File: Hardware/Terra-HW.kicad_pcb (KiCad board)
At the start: 4 copper layers, 77 x 68 mm, 97 parts, among them J1 GT-USB-7010ASV, J2 S2B-PH-SM4-TB, J3 0532610271, J5 B8B-PH-SM4-TB, J6 0532610671, Q1 DMP3099L, Q2 2N7002, Q3 2N7002, SW2 KMR231NG, SW3 KMR231NG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

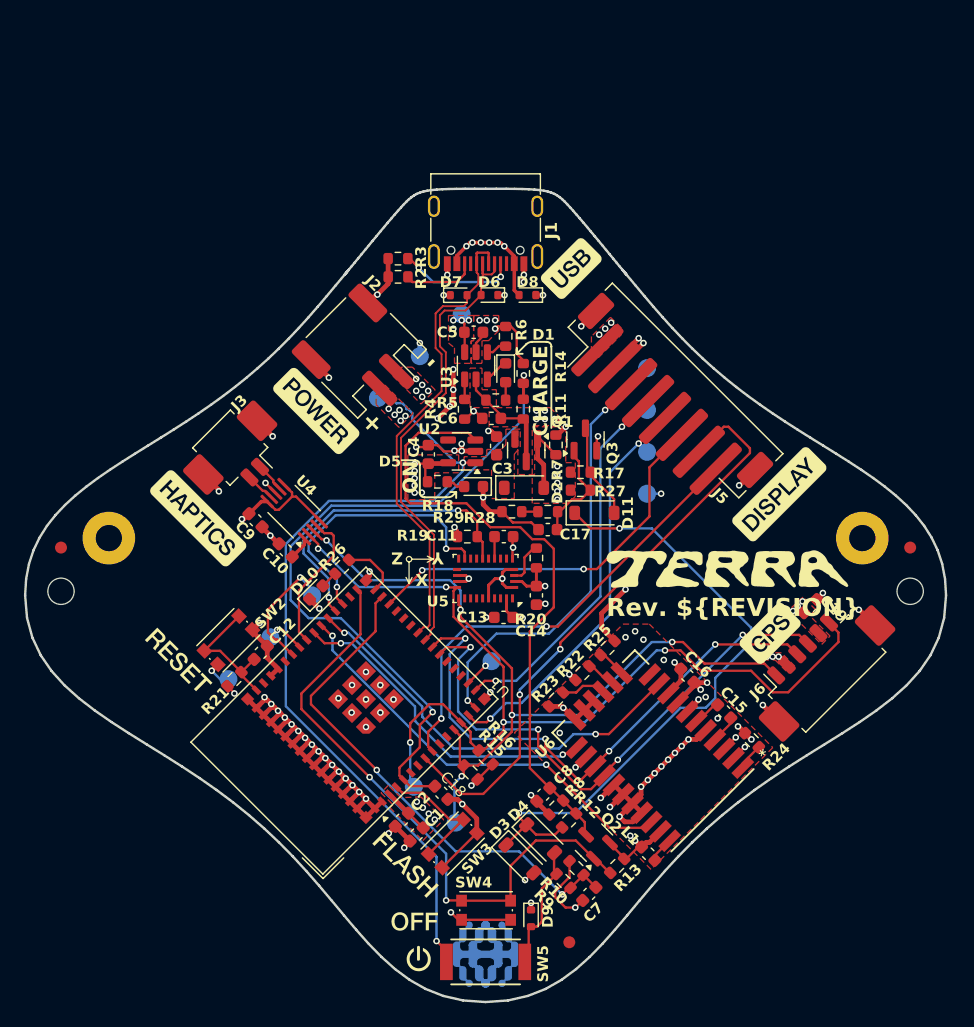
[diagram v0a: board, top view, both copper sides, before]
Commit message: update board outline and flip 180
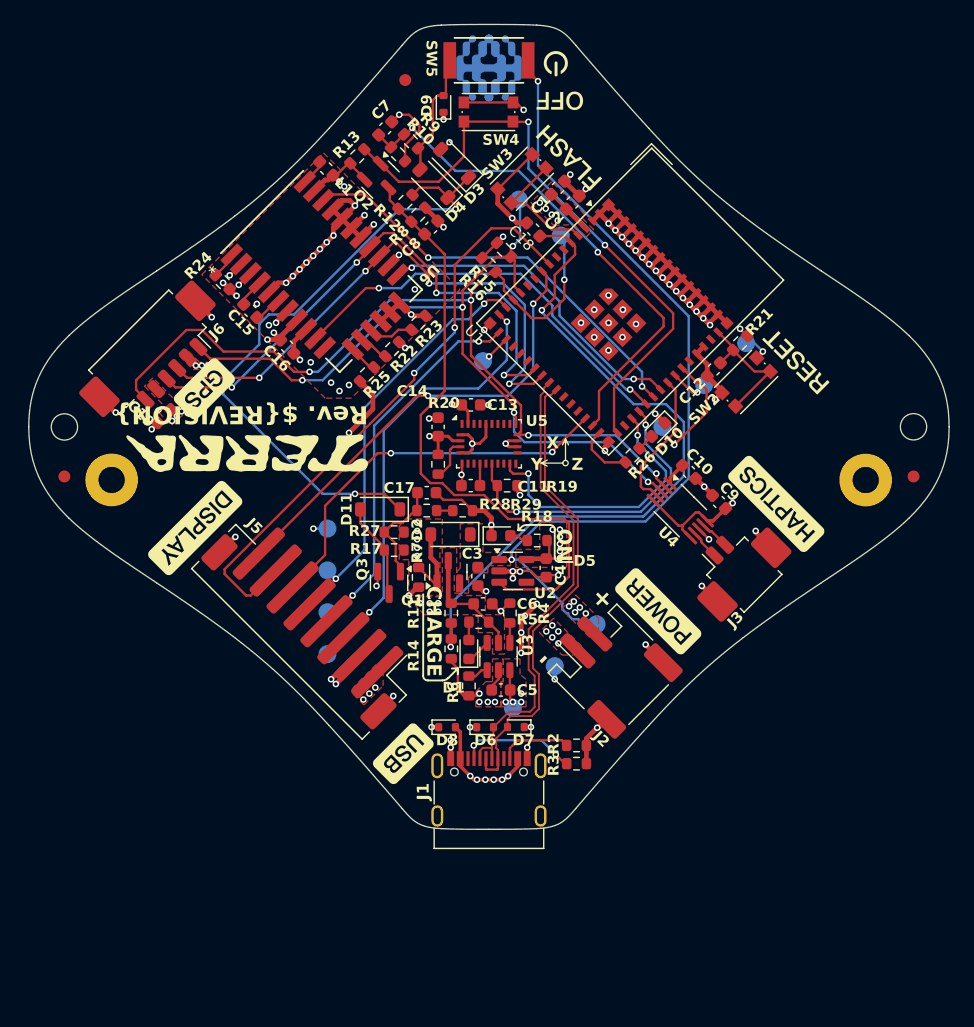
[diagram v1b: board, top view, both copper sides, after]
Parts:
- moved SW5 75.4 mm to (150.0, 61.4), turned to 180 degrees
- moved FID2 73.4 mm to (143.0, 63.1), turned to 180 degrees
- moved H2 72.6 mm to (185.5, 92.1), turned to 180 degrees
- moved H1 72.0 mm to (114.6, 92.1), turned to 180 degrees
- moved FID3 71.5 mm to (185.5, 96.2), turned to 180 degrees
- moved FID1 71.0 mm to (114.5, 96.2), turned to 180 degrees
- moved D9 68.5 mm to (146.2, 65.1), turned to 90 degrees
- moved SW4 66.7 mm to (150.0, 65.7), turned to 0 degrees
- moved C7 66.2 mm to (141.4, 67.1), turned to 45 degrees
- moved H3 63.5 mm to (181.5, 96.5), turned to 180 degrees
- moved L1 63.3 mm to (136.4, 70.5), turned to -45 degrees
- moved R13 63.2 mm to (139.0, 69.4), turned to 45 degrees
- moved R9 63.1 mm to (143.5, 68.2), turned to -45 degrees
- moved H4 62.9 mm to (118.5, 96.5), turned to 180 degrees
- moved J6 62.0 mm to (121.8, 85.9), turned to -135 degrees
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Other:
- board size 77 x 68 mm -> 76.9 x 67.3 mm

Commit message: pcb: initial layout of TESSO gps
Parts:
- removed J6: 0532610671, Connector_Molex:Molex_PicoBlade_53261-0671_1x06-1MP_P1.25mm_Horizontal
- removed R23: 10k, Resistor_SMD:R_0603_1608Metric
- removed R24: 0R, Resistor_SMD:R_0603_1608Metric
- added J4: Conn_Coaxial, Connector_Coaxial:U.FL_Molex_MCRF_73412-0110_Vertical, F.Cu at (123.7, 83.6)
- added U7: BGA725L6, Symbols:BGA-6_2x3_0.8x1.2mm, F.Cu at (129.4, 86.0)
- added U8: B4327, Symbols:SOIC-5 B4327, F.Cu at (128.3, 84.7)
- C15, C16: value 22p -> 120p; footprint Capacitor_SMD:C_0603_1608Metric -> Capacitor_SMD:C_0402_1005Metric
- C19: value 1u -> 0.1u
- L1: value 1.8n -> 5.6n; footprint Inductor_SMD:L_0603_1608Metric -> Inductor_SMD:L_0402_1005Metric
- U6: value M20048-1 -> TESEO-LIV3F; footprint M20048-1:QFN28_M20048-1_ANT -> TESO-LIV3F:LCC-18_9P7X10P1_STM
- moved L1 19.2 mm to (127.5, 87.5)
- moved C19 11.4 mm to (130.8, 83.0), turned to -45 degrees
- moved R22 9.98 mm to (132.0, 85.6), turned to -135 degrees
- moved C16 7.14 mm to (126.1, 86.0), turned to 135 degrees
- moved C15 2.94 mm to (127.2, 82.8)
- moved U6 1.75 mm to (134.6, 78.0), turned to -135 degrees
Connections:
- C15 pad 1: Net-(U6-ANT_OUT) -> Net-(U6-RF_IN)
- C15 pad 2: Net-(U6-RF_IN) -> Net-(U8-RF_{OUT})
- C16 pad 1: +3.3V -> Net-(C16-Pad1)
- C16 pad 2: GND -> Net-(J4-In)
- C19 pad 1: +3.3V -> +3.3V_RF
- J2 pad 1: GND -> VBAT
- J2 pad 2: VBAT -> GND
- L1 pad 1: Net-(U6-AT2) -> Net-(C16-Pad1)
- L1 pad 2: GND -> Net-(U7-A_{IN})
- R22 pad 1: /Peripehrals/GPS_BAUD1 -> GND
- R22 pad 2: GND -> /Peripehrals/ANT_EN
- R25 pad 2: /Peripehrals/GPS_VBACKUP -> /Peripehrals/GPS_VBAT
- U6 pad 1: Net-(U6-AT1) -> GND
- U6 pad 10: /Microcontroller/GPS_~{RST} -> GND
- U6 pad 11: unconnected-(U6-TM-Pad11) -> Net-(U6-RF_IN)
- U6 pad 12: /Peripehrals/GPS_VBACKUP -> GND
- U6 pad 13: /Peripehrals/GPS_BAUD1 -> /Peripehrals/ANT_EN
- U6 pad 14: /Peripehrals/GPS_BAUD2 -> +3.3V_RF
- U6 pad 15: GND -> unconnected-(U6-RESERVED-Pad15)
- U6 pad 16: GND -> /Microcontroller/I2C_SDA
- U6 pad 17: GND -> /Microcontroller/I2C_SCL
- U6 pad 18: /Microcontroller/GPS_FIX -> unconnected-(U6-RESERVED-Pad18)
- U6 pad 2: GND -> /Microcontroller/U1RXD
- U6 pad 3: GND -> /Microcontroller/U1TXD
- U6 pad 4: Net-(U6-ANT_OUT) -> /Microcontroller/GPS_FIX
- U6 pad 5: GND -> /Microcontroller/GPS_STBY
- U6 pad 6: Net-(U6-RF_IN) -> /Peripehrals/GPS_VBAT
- U6 pad 7: GND -> +3.3V
- U6 pad 9: GND -> /Microcontroller/GPS_~{RST}
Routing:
- net GND: track 192.8 -> 148.8 mm, vias 115 -> 105
- net /Microcontroller/U1TXD: track 46.7 -> 25.2 mm, vias 4 -> 2
- net /Microcontroller/U1RXD: track 46.5 -> 26.1 mm, vias 4 -> 2
- net /Microcontroller/I2C_SCL: track 79.7 -> 60.1 mm, vias 5 -> 4
- net /Peripehrals/GPS_VBAT: track 0.00 -> 10.4 mm
- net /Microcontroller/I2C_SDA: track 68.3 -> 58.5 mm, vias 5 -> 4
- net /Peripehrals/ANT_EN: track 0.00 -> 8.54 mm, vias 0 -> 3
- net Net-(D11-K): track 53.6 -> 46.0 mm
- net +3.3V_RF: track 0.00 -> 6.05 mm
- net /Microcontroller/GPS_FIX: track 27.3 -> 32.7 mm
- net Net-(U7-A_{IN}): track 0.00 -> 4.91 mm
- net /Microcontroller/GPS_~{RST}: track 34.9 -> 39.5 mm
- net +3.3V: track 40.2 -> 36.4 mm, vias 27 -> 25
- net /Peripehrals/GPS_BAUD2: track 3.09 -> 0.00 mm
- net Net-(U6-RF_IN): track 1.88 -> 4.75 mm
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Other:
- board text added: "0.0175 mm"
- board text added: "0.196 mm"
- board text added: "1.03 mm"
- board text added: "1.5470 mm"
- board text added: "4.6"
- board text added: "4.74"
- board text added: "76.9462 mm x 67.2932 mm"
- board text added: "Dielectric 1"
- board text added: "Dielectric 2"
- board text added: "Dielectric 3"
- board text added: "NOTE: STACKUP BASED ON PCBWAY 4-LAYER 70% RESIDUAL COPPER RATIO DEFAULT STACK."
- board text added: "Yes"
- board text removed: "0.0152 mm"
- board text removed: "0.0994 mm"
- board text removed: "1.265 mm"
- board text removed: "1.5842 mm"
- board text removed: "4.5"
- board text removed: "77.0000 mm x 68.0000 mm"
- board text removed: "Dielectric"

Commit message: pcb: other cleanup
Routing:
- net GND: track 148.8 -> 142.9 mm, vias 105 -> 106

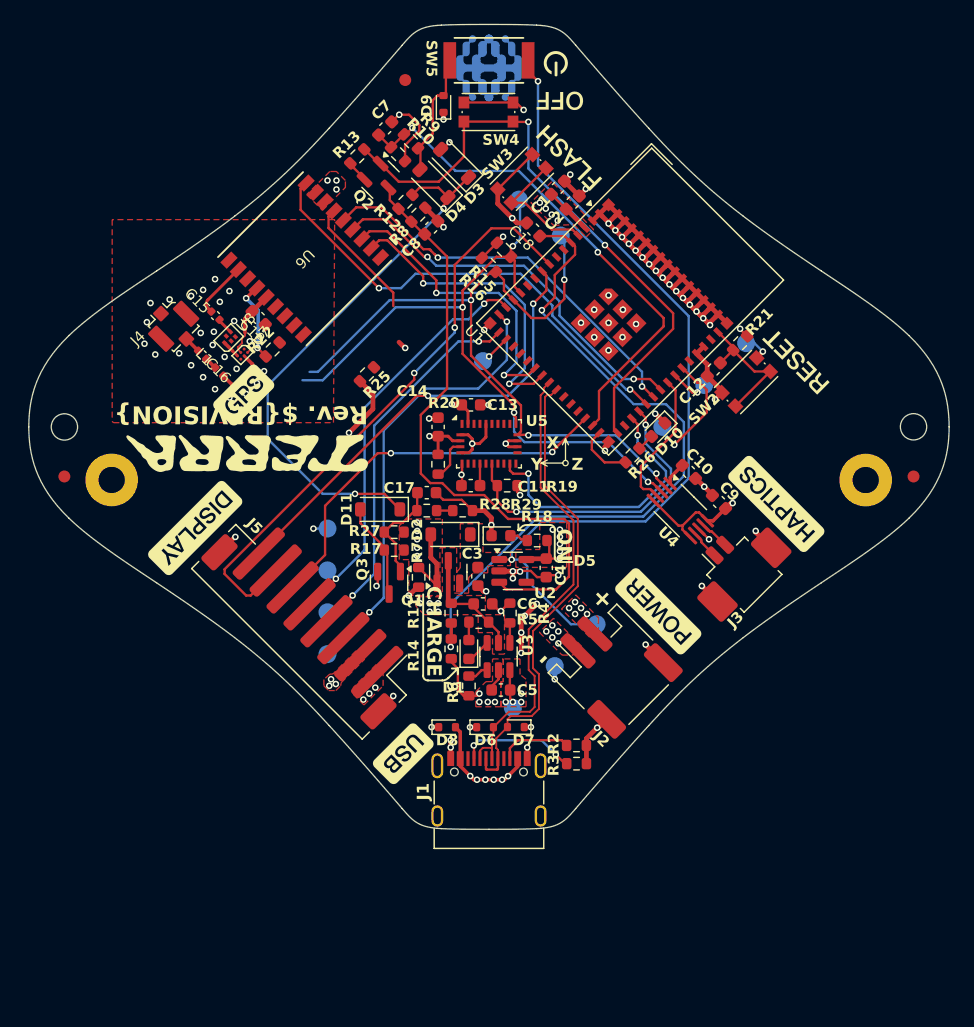
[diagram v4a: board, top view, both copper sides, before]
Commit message: pcb: gps cleanup
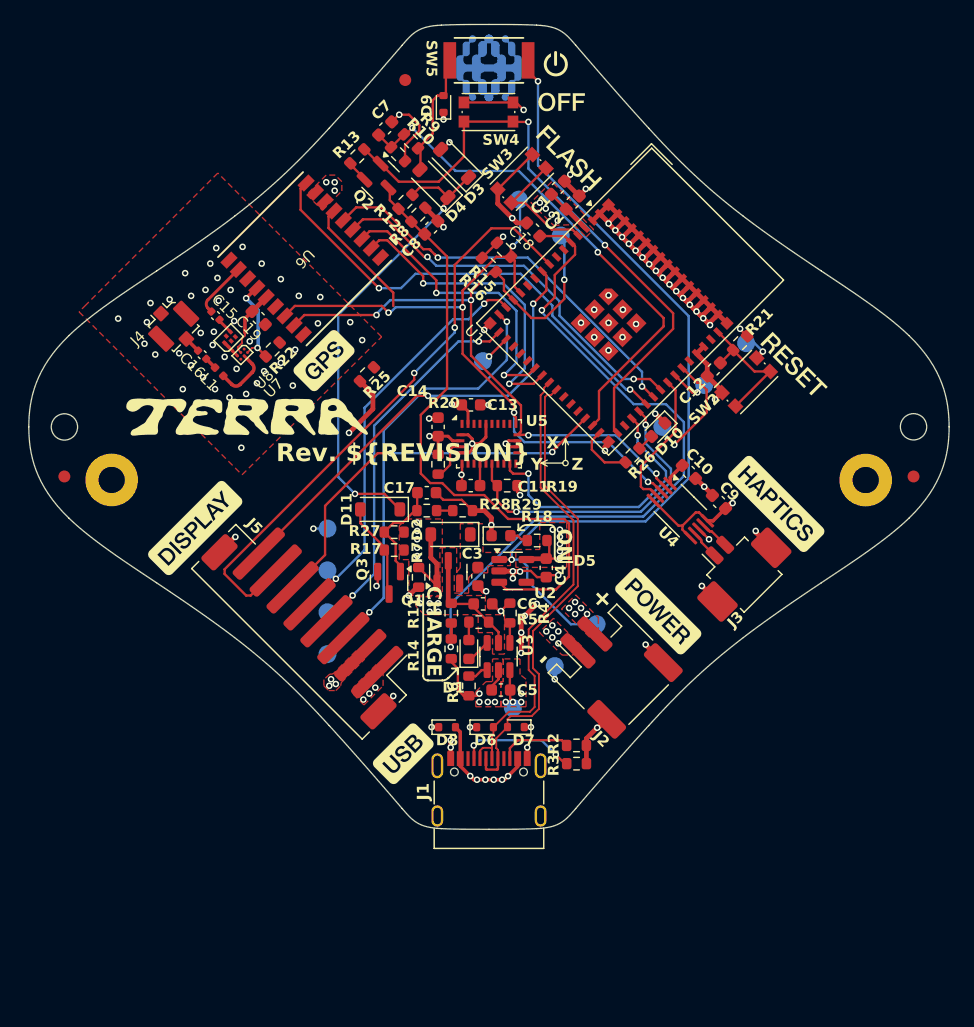
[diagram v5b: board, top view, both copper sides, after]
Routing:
- net Net-(D11-K): track 46.0 -> 39.6 mm
- net /Peripehrals/ANT_EN: track 8.54 -> 7.83 mm, vias 3 -> 2
- net /Microcontroller/I2C_SDA: track 58.5 -> 58.2 mm, vias 4 -> 5
- net /Microcontroller/I2C_SCL: track 60.1 -> 59.9 mm, vias 4 -> 5
- net GND: vias 106 -> 123
